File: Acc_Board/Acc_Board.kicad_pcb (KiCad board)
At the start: 2 copper layers, 139.7 x 88.9 mm, 85 parts, among them J1 AIRs Power, J10 Conn_01x02_Pin, J12 776087-1, J2 IsoSPI, J3 IMD BAT, J4 HV Power, J5 HVIL, J6 IMD, J7 Current Sensor, J8 Fans, J9 Shutdown IL, K1 Relay_SPST-NO, K2 Latching Relay, Q1 STS6NF20V, Q2 STS6NF20V, Q3 STS6NF20V, Q4 STS6NF20V, U1 ISO1050DUB, U10 DK1A1B-12V, U11 TLP3122AE, U12 LTC6820, U13 NAND, U14 TLP3122AE, U15 MCP6004, U16 TLP3122AE, U2 NUCLEO-L432KC, U3 LM555N, U4 PQDE6W-Q110-S5-H-D, U5 R-78B5.0-2.0, U6 TLP3122AE, U7 DK1A1B-12V, U8 LM7809_TO220, U9 TLP3122AE

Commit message: Minor acc board fixes
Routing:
- net /CAN1_RD: track 30.4 -> 31.1 mm, vias 0 -> 1
- net /BMS_FAULT_5V: vias 11 -> 9
- net /Precharge_Relay: vias 4 -> 2
- net /CAN1_TD: vias 2 -> 0
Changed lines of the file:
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@@
   (segment (start 88.63 81.28) (end 89.375 81.28) (width 0.2) (layer "F.Cu") (net 39))
   (segment (start 88.63 81.01) (end 87.63 80.01) (width 0.2) (layer "F.Cu") (net 39))
-  (segment (start 71.12 53.34) (end 57.15 53.34) (width 0.25) (layer "F.Cu") (net 40))
   (segment (start 74.93 53.34) (end 96.52 53.34) (width 0.25) (layer "F.Cu") (net 40))
+  (segment (start 43.18 55.88) (end 45.72 53.34) (width 0.25) (layer "F.Cu") (net 40))
   (segment (start 96.52 53.34) (end 97.155 53.975) (width 0.25) (layer "F.Cu") (net 40))
-  (segment (start 45.72 53.34) (end 43.18 55.88) (width 0.25) (layer "F.Cu") (net 40))
-  (segment (start 54.61 53.34) (end 45.72 53.34) (width 0.25) (layer "F.Cu") (net 40))
+  (segment (start 45.72 53.34) (end 71.12 53.34) (width 0.25) (layer "F.Cu") (net 40))
   (segment (start 97.155 53.975) (end 99.1362 53.975) (width 0.25) (layer "F.Cu") (net 40))
   (via (at 71.12 53.34) (size 0.8) (drill 0.4) (layers "F.Cu" "B.Cu") (net 40))
-  (via (at 57.15 53.34) (size 0.8) (drill 0.4) (layers "F.Cu" "B.Cu") (net 40))
   (via (at 74.93 53.34) (size 0.8) (drill 0.4) (layers "F.Cu" "B.Cu") (net 40))
-  (via (at 54.61 53.34) (size 0.8) (drill 0.4) (layers "F.Cu" "B.Cu") (net 40))
   (segment (start 71.12 53.34) (end 74.93 53.34) (width 0.25) (layer "B.Cu") (net 40))
-  (segment (start 57.15 53.34) (end 54.61 53.34) (width 0.25) (layer "B.Cu") (net 40))
   (segment (start 62.1538 85.0138) (end 62.1538 85.725) (width 0.25) (layer "F.Cu") (net 41))
   (segment (start 61.595 84.455) (end 62.1538 85.0138) (width 0.25) (layer "F.Cu") (net 41))
@@
   (segment (start 25.4 31.5175) (end 25.6325 31.75) (width 0.25) (layer "F.Cu") (net 68))
   (segment (start 25.4 31.9825) (end 25.4 40.64) (width 0.5) (layer "F.Cu") (net 68))
-  (segment (start 58.42 50.8) (end 55.88 53.34) (width 0.25) (layer "F.Cu") (net 76))
-  (segment (start 58.42 50.8) (end 72.39 50.8) (width 0.25) (layer "F.Cu") (net 76))
-  (segment (start 55.88 53.34) (end 55.88 55.88) (width 0.25) (layer "F.Cu") (net 76))
+  (segment (start 57.15 50.8) (end 72.39 50.8) (width 0.25) (layer "F.Cu") (net 76))
   (segment (start 76.2 45.72) (end 76.2 46.99) (width 0.25) (layer "F.Cu") (net 76))
   (segment (start 76.2 46.99) (end 72.39 50.8) (width 0.25) (layer "F.Cu") (net 76))
   (segment (start 74.93 44.45) (end 76.2 45.72) (width 0.25) (layer "F.Cu") (net 76))
   (segment (start 74.93 42.625) (end 74.93 44.45) (width 0.25) (layer "F.Cu") (net 76))
-  (segment (start 55.88 52.07) (end 39.37 52.07) (width 0.25) (layer "F.Cu") (net 77))
-  (segment (start 39.37 52.07) (end 35.56 55.88) (width 0.25) (layer "F.Cu") (net 77))
+  (via (at 57.15 50.8) (size 0.8) (drill 0.4) (layers "F.Cu" "B.Cu") (net 76))
+  (segment (start 55.88 52.07) (end 55.88 55.88) (width 0.25) (layer "B.Cu") (net 76))
+  (segment (start 57.15 50.8) (end 55.88 52.07) (width 0.25) (layer "B.Cu") (net 76))
+  (segment (start 35.56 55.88) (end 39.37 52.07) (width 0.25) (layer "F.Cu") (net 77))
+  (segment (start 72.39 52.07) (end 77.47 46.99) (width 0.25) (layer "F.Cu") (net 77))
   (segment (start 77.47 46.99) (end 77.47 42.625) (width 0.25) (layer "F.Cu") (net 77))
-  (segment (start 58.42 52.07) (end 72.39 52.07) (width 0.25) (layer "F.Cu") (net 77))
-  (segment (start 72.39 52.07) (end 77.47 46.99) (width 0.25) (layer "F.Cu") (net 77))
-  (via (at 55.88 52.07) (size 0.8) (drill 0.4) (layers "F.Cu" "B.Cu") (net 77))
-  (via (at 58.42 52.07) (size 0.8) (drill 0.4) (layers "F.Cu" "B.Cu") (net 77))
-  (segment (start 55.88 52.07) (end 58.42 52.07) (width 0.25) (layer "B.Cu") (net 77))
+  (segment (start 39.37 52.07) (end 72.39 52.07) (width 0.25) (layer "F.Cu") (net 77))
   (segment (start 50.8 33.02) (end 48.26 33.02) (width 0.25) (layer "F.Cu") (net 78))
   (segment (start 50.8 35.56) (end 49.53 36.83) (width 0.25) (layer "F.Cu") (net 78))
@@
   (segment (start 100.33 29.21) (end 100.33 45.72) (width 0.25) (layer "F.Cu") (net 88))
   (segment (start 96.52 49.53) (end 91.44 49.53) (width 0.25) (layer "F.Cu") (net 88))
-  (segment (start 69.85 54.61) (end 57.15 54.61) (width 0.25) (layer "F.Cu") (net 88))
   (segment (start 100.33 24.0475) (end 100.33 24.13) (width 0.25) (layer "F.Cu") (net 88))
   (segment (start 21.833 59.66) (end 23.073 58.42) (width 0.25) (layer "F.Cu") (net 88))
   (segment (start 88.9 52.07) (end 83.82 52.07) (width 0.25) (layer "F.Cu") (net 88))
   (segment (start 23.073 58.42) (end 27.94 58.42) (width 0.25) (layer "F.Cu") (net 88))
+  (segment (start 46.99 54.61) (end 69.85 54.61) (width 0.25) (layer "F.Cu") (net 88))
   (segment (start 91.44 49.53) (end 88.9 52.07) (width 0.25) (layer "F.Cu") (net 88))
   (segment (start 74.93 52.07) (end 72.39 54.61) (width 0.25) (layer "F.Cu") (net 88))
@@
   (segment (start 27.97 58.45) (end 27.94 58.42) (width 0.25) (layer "F.Cu") (net 88))
   (segment (start 30.48 58.42) (end 31.75 57.15) (width 0.25) (layer "F.Cu") (net 88))
-  (segment (start 54.61 54.61) (end 46.99 54.61) (width 0.25) (layer "F.Cu") (net 88))
-  (via (at 57.15 54.61) (size 0.8) (drill 0.4) (layers "F.Cu" "B.Cu") (net 88))
   (via (at 100.33 29.21) (size 0.8) (drill 0.4) (layers "F.Cu" "B.Cu") (net 88))
   (via (at 72.39 54.61) (size 0.8) (drill 0.4) (layers "F.Cu" "B.Cu") (net 88))
   (via (at 46.99 54.61) (size 0.8) (drill 0.4) (layers "F.Cu" "B.Cu") (net 88))
-  (via (at 54.61 54.61) (size 0.8) (drill 0.4) (layers "F.Cu" "B.Cu") (net 88))
   (via (at 83.82 52.07) (size 0.8) (drill 0.4) (layers "F.Cu" "B.Cu") (net 88))
   (via (at 31.75 54.61) (size 0.8) (drill 0.4) (layers "F.Cu" "B.Cu") (net 88))
@@
   (segment (start 100.33 24.13) (end 100.33 29.21) (width 0.25) (layer "B.Cu") (net 88))
   (segment (start 72.39 54.61) (end 69.85 54.61) (width 0.25) (layer "B.Cu") (net 88))
-  (segment (start 57.15 54.61) (end 54.61 54.61) (width 0.25) (layer "B.Cu") (net 88))
   (segment (start 83.82 52.07) (end 83.81 52.08) (width 0.25) (layer "B.Cu") (net 88))
   (segment (start 67.31 58.42) (end 74.93 50.8) (width 0.25) (layer "F.Cu") (net 89))
   (segment (start 91.44 48.26) (end 96.52 48.26) (width 0.25) (layer "F.Cu") (net 89))
   (segment (start 93.345 18.415) (end 99.06 24.13) (width 0.25) (layer "F.Cu") (net 89))
+  (segment (start 88.9 66.055) (end 88.9 54.61) (width 0.25) (layer "F.Cu") (net 89))
   (segment (start 88.9 50.8) (end 91.44 48.26) (width 0.25) (layer "F.Cu") (net 89))
   (segment (start 88.9 73.66) (end 74.93 73.66) (width 0.25) (layer "F.Cu") (net 89))
   (segment (start 91.43 71.125) (end 91.43 68.585) (width 0.25) (layer "F.Cu") (net 89))
   (segment (start 52.07 58.42) (end 46.99 58.42) (width 0.25) (layer "F.Cu") (net 89))
-  (segment (start 90.17 67.325) (end 90.17 63.5) (width 0.25) (layer "F.Cu") (net 89))
   (segment (start 88.9 50.8) (end 74.93 50.8) (width 0.25) (layer "F.Cu") (net 89))
   (segment (start 88.74 16.4575) (end 90.6975 18.415) (width 0.25) (layer "F.Cu") (net 89))
@@
   (segment (start 71.12 80.01) (end 71.12 81.386908) (width 0.25) (layer "F.Cu") (net 89))
   (segment (start 99.06 45.72) (end 99.06 29.21) (width 0.25) (layer "F.Cu") (net 89))
-  (segment (start 88.9 62.23) (end 88.9 54.61) (width 0.25) (layer "F.Cu") (net 89))
-  (segment (start 90.17 63.5) (end 88.9 62.23) (width 0.25) (layer "F.Cu") (net 89))
   (segment (start 40.67 63.47) (end 40.64 63.47) (width 0.25) (layer "F.Cu") (net 89))
   (segment (start 90.6975 18.415) (end 93.345 18.415) (width 0.25) (layer "F.Cu") (net 89))
   (segment (start 91.43 71.125) (end 91.43 71.13) (width 0.25) (layer "F.Cu") (net 89))
+  (segment (start 91.43 68.585) (end 88.9 66.055) (width 0.25) (layer "F.Cu") (net 89))
   (segment (start 67.31 58.42) (end 59.69 58.42) (width 0.25) (layer "F.Cu") (net 89))
-  (segment (start 91.43 68.585) (end 90.17 67.325) (width 0.25) (layer "F.Cu") (net 89))
   (via (at 99.06 24.13) (size 0.8) (drill 0.4) (layers "F.Cu" "B.Cu") (net 89))
   (via (at 99.06 45.72) (size 0.8) (drill 0.4) (layers "F.Cu" "B.Cu") (net 89))

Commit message: Acc board changes
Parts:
- moved G*** 3.81 mm to (122.6, 33.1)
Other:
- board text added: "FS-2 Acc Board Formula Slug V 1.5 Designed By Cole Lewis"
- board text removed: "FS-2 Acc Board Formula Slug V 1.5"
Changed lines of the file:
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@@
   )
   (footprint "1FS_2_Global_Footprint_Library:FORMULA SLUG" (layer "F.Cu")
-    (at 126.40258 33.078544)
+    (at 122.59258 33.078544)
     (attr board_only exclude_from_pos_files exclude_from_bom)
     (fp_text reference "G***" (at 0 0) (layer "F.SilkS") hide
@@
     (effects (font (size 1 1) (thickness 0.15)))
   )
-  (gr_text "FS-2 Acc Board\nFormula Slug\nV 1.5" (at 124.46 33.02) (layer "F.SilkS")
+  (gr_text "FS-2 Acc Board\nFormula Slug\nV 1.5\nDesigned By Cole Lewis" (at 120.65 33.02) (layer "F.SilkS")
     (effects (font (size 1 1) (thickness 0.15)) (justify left))
   )

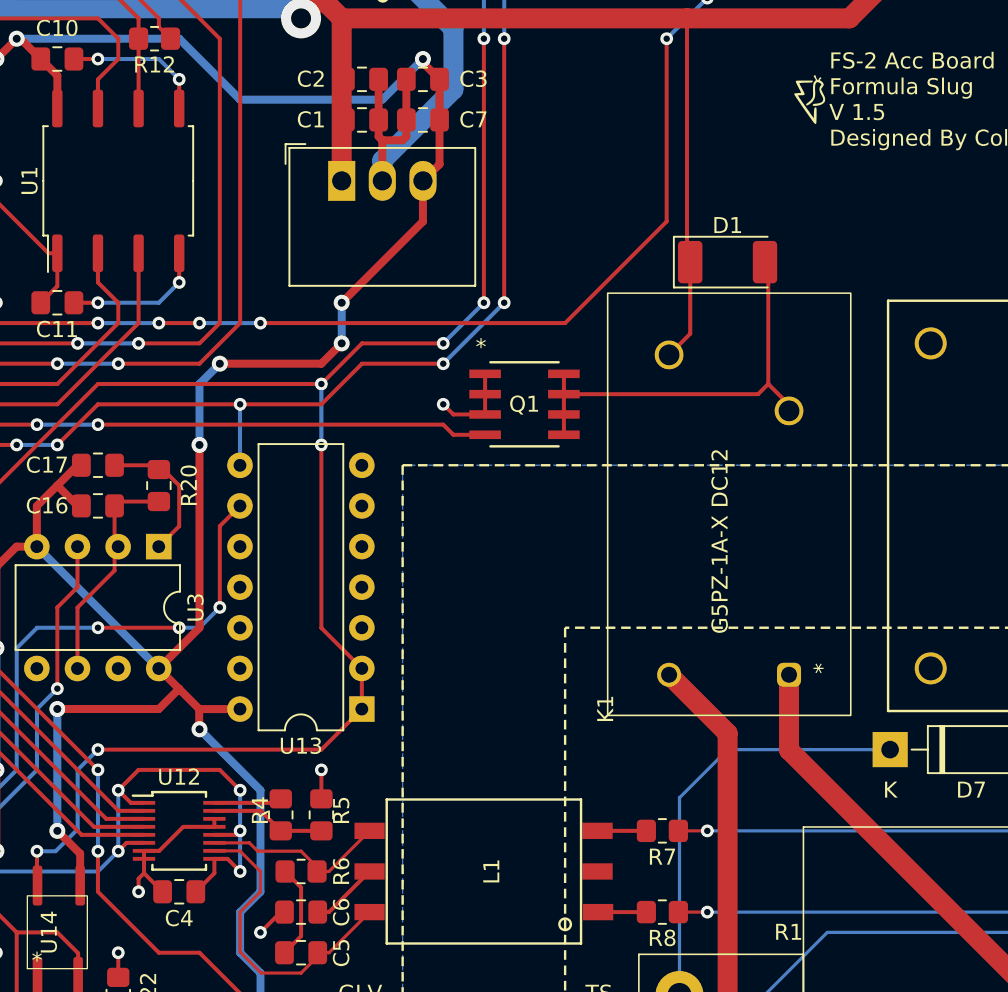
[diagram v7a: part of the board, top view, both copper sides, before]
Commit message: fixed nand gate on acc board
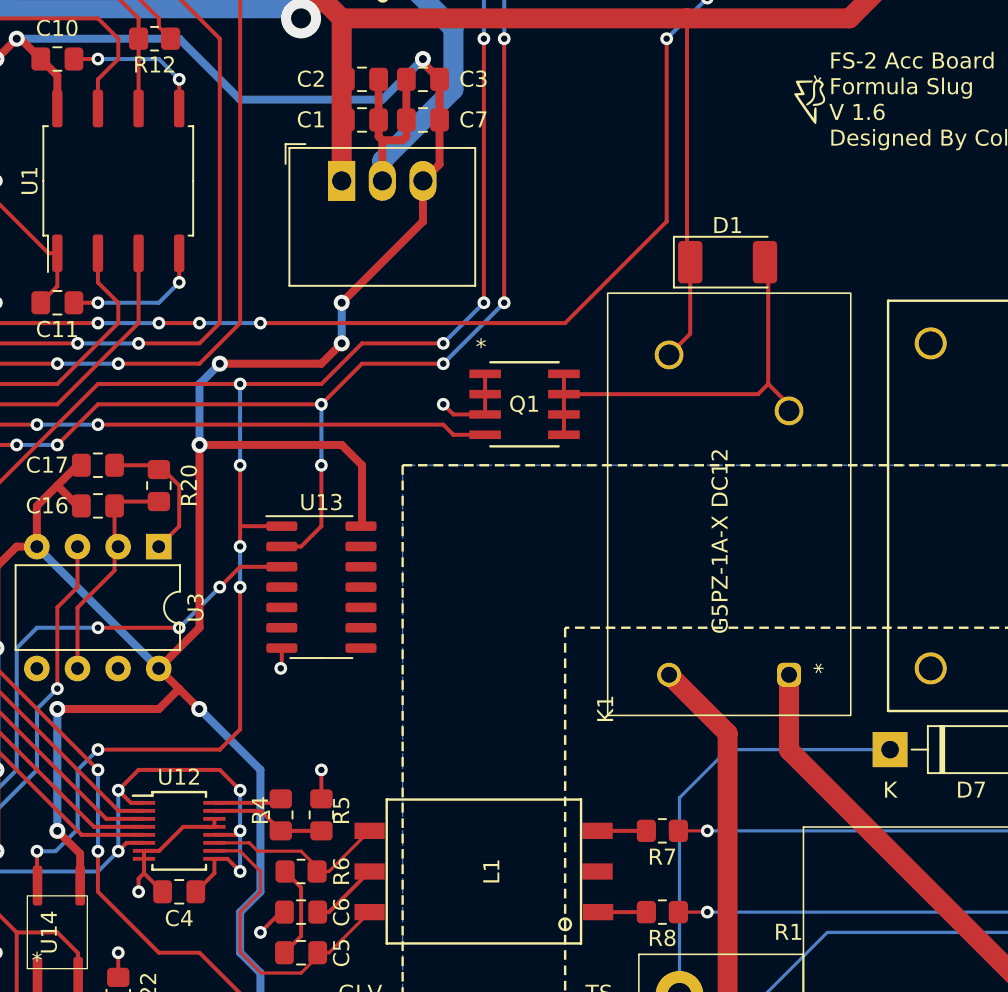
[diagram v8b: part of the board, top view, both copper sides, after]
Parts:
- U13: value NAND -> HEF4093B; footprint Package_DIP:DIP-14_W7.62mm -> Package_SO:SOIC-14_3.9x8.7mm_P1.27mm
- moved U13 8.03 mm to (88.9, 63.5), turned to 0 degrees
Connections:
- U13 pad 2: /IMD_FAULT_5V -> /BMS_FAULT_5V
- U13 pad 3: (no net) -> Net-(U11-Pad3)
- U13 pad 8: /BMS_FAULT_5V -> (no net)
- U13 pad 9: Net-(U11-Pad3) -> (no net)
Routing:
- net +5V: track 248.1 -> 260.1 mm
- net /BMS_FAULT_5V: track 126.7 -> 133.5 mm, vias 9 -> 10
- net /IMD_FAULT_5V: track 149.8 -> 144.5 mm, vias 12 -> 14
- net Net-(U11-Pad3): track 35.1 -> 33.2 mm
- net GND: track 206.0 -> 207.3 mm, vias 23 -> 24
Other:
- board text added: "FS-2 Acc Board Formula Slug V 1.6 Designed By Cole Lewis"
- board text removed: "FS-2 Acc Board Formula Slug V 1.5 Designed By Cole Lewis"
